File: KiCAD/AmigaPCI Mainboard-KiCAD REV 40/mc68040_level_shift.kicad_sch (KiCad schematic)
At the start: 28 parts, among them U800 74LVC1G17, U801 74LVC1G17, U802 SN74LVC16T245DLR, U803 SN74LVC16T245DLR, U804 SN74LVC16T245DLR, U805 SN74LVC16T245DLR, U806 74LVC245, U807 74LVC245, U808 74LVC245, U809 74LVC245, U810 74LVC245, U811 74LVC245

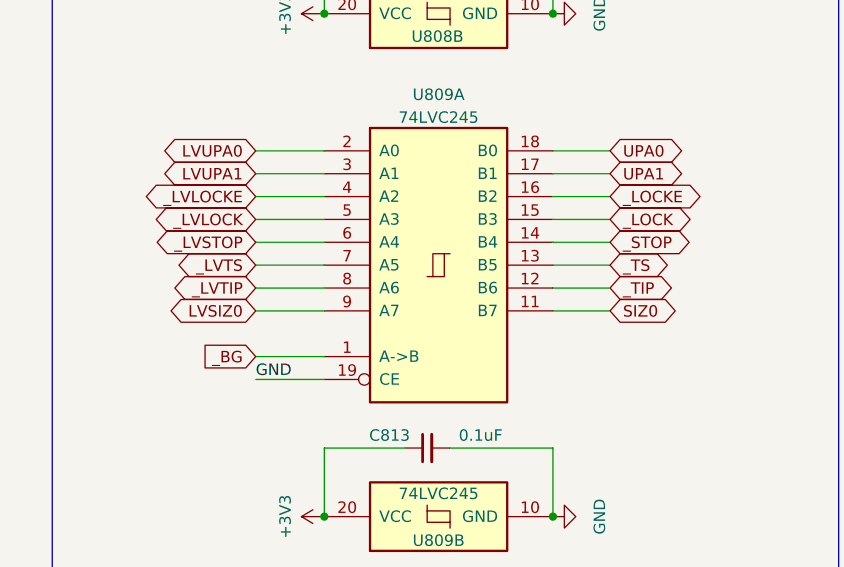
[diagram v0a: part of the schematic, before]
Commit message: Schematic Changes for Rev 4.0 03-JUL-2024
Remove _TIP, replace with GND at CN200.
Add _TS to U712.
Remove _TCI and _TBI from U409.
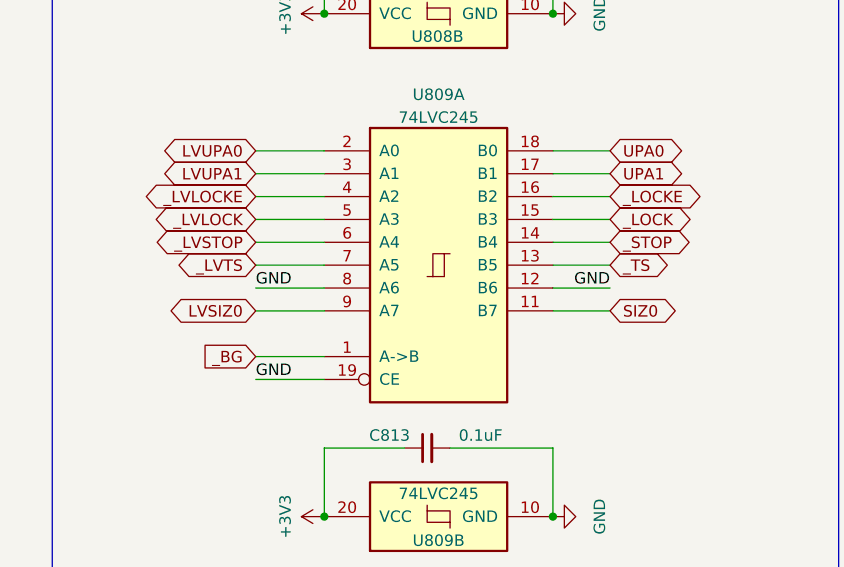
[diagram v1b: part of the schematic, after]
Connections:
- net _LVTIP is gone; now on net GND: U809.8 (A6)
- net _TIP is gone; now on net GND: U809.12 (B6)
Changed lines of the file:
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@@
 	(title_block
 		(title "AMIGA PCI")
-		(date "2024-06-29")
+		(date "2024-07-03")
 		(rev "4.0")
 	)
@@
 		)
 	)
+	(label "GND"
+		(at 274.32 228.6 180)
+		(fields_autoplaced yes)
+		(effects
+			(font
+				(size 1.27 1.27)
+			)
+			(justify right bottom)
+		)
+	)
 	(label "A7"
 		(at 170.18 63.5 180)
@@
 		)
 	)
+	(label "GND"
+		(at 234.95 228.6 0)
+		(fields_autoplaced yes)
+		(effects
+			(font
+				(size 1.27 1.27)
+			)
+			(justify left bottom)
+		)
+	)
 	(label "LVD11"
 		(at 31.75 91.44 0)
@@
 		)
 	)
-	(global_label "_TIP"
-		(shape bidirectional)
-		(at 274.32 228.6 0)
-		(fields_autoplaced yes)
-		(effects
-			(font
-				(size 1.27 1.27)
-			)
-			(justify left)
-		)
-		(property "Intersheetrefs" "${INTERSHEET_REFS}"
-			(at 282.2265 228.6 0)
-			(effects
-				(font
-					(size 1.27 1.27)
-				)
-				(justify left)
-			)
-		)
-	)
 	(global_label "LVDRA4-3"
 		(shape output)
@@
 			)
 		)
-	)
-	(global_label "_LVTIP"
-		(shape bidirectional)
-		(at 234.95 228.6 180)
-		(fields_autoplaced yes)
-		(effects
-			(font
-				(size 1.27 1.27)
-			)
-			(justify right)
-		)
-		(property "Intersheetrefs" "${INTERSHEET_REFS}"
-			(at 224.9268 228.6 0)
-			(effects
-				(font
-					(size 1.27 1.27)
-				)
-				(justify right)
-			)
-		)
